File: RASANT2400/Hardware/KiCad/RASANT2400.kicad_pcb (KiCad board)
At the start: 2 copper layers, 60.3 x 51.4 mm, 0 parts

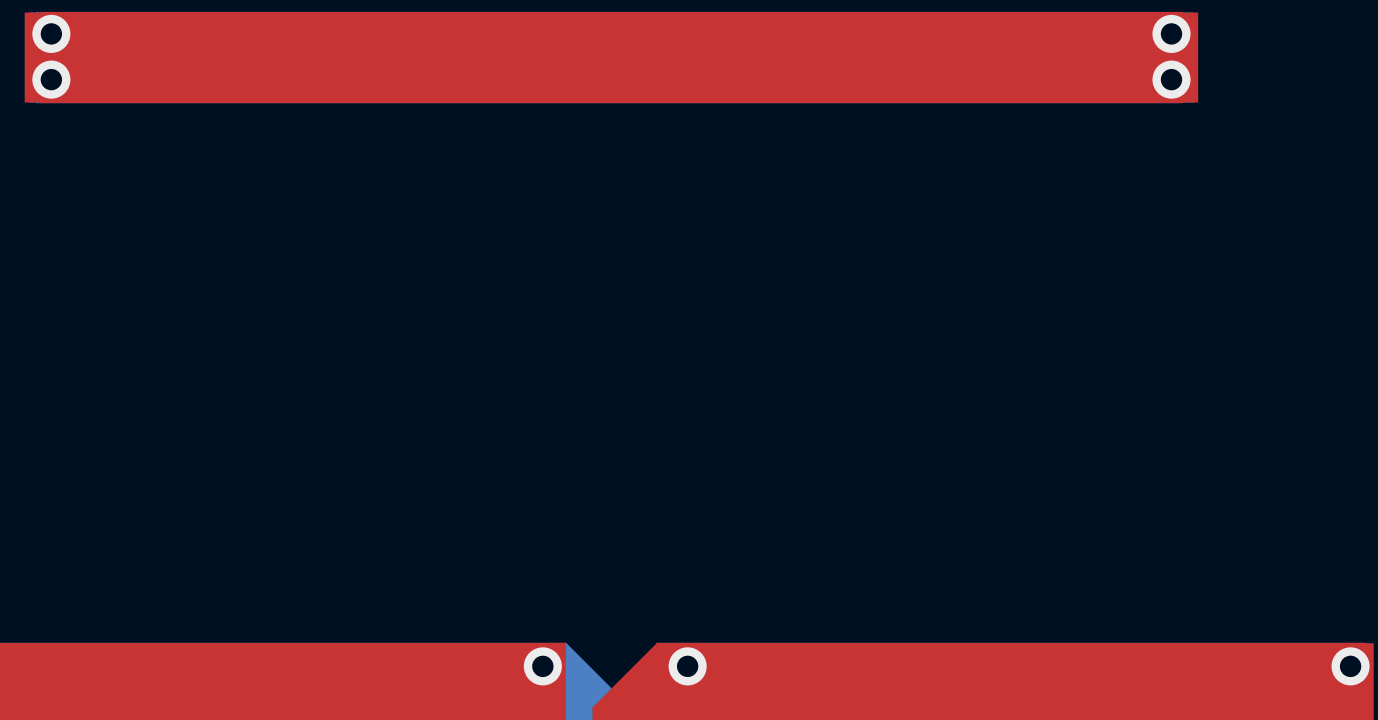
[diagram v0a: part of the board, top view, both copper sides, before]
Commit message: Changed license to CERN Open Hardware Licence Version 2 - Strongly Reciprocal. Changed position of the logos on PCB.
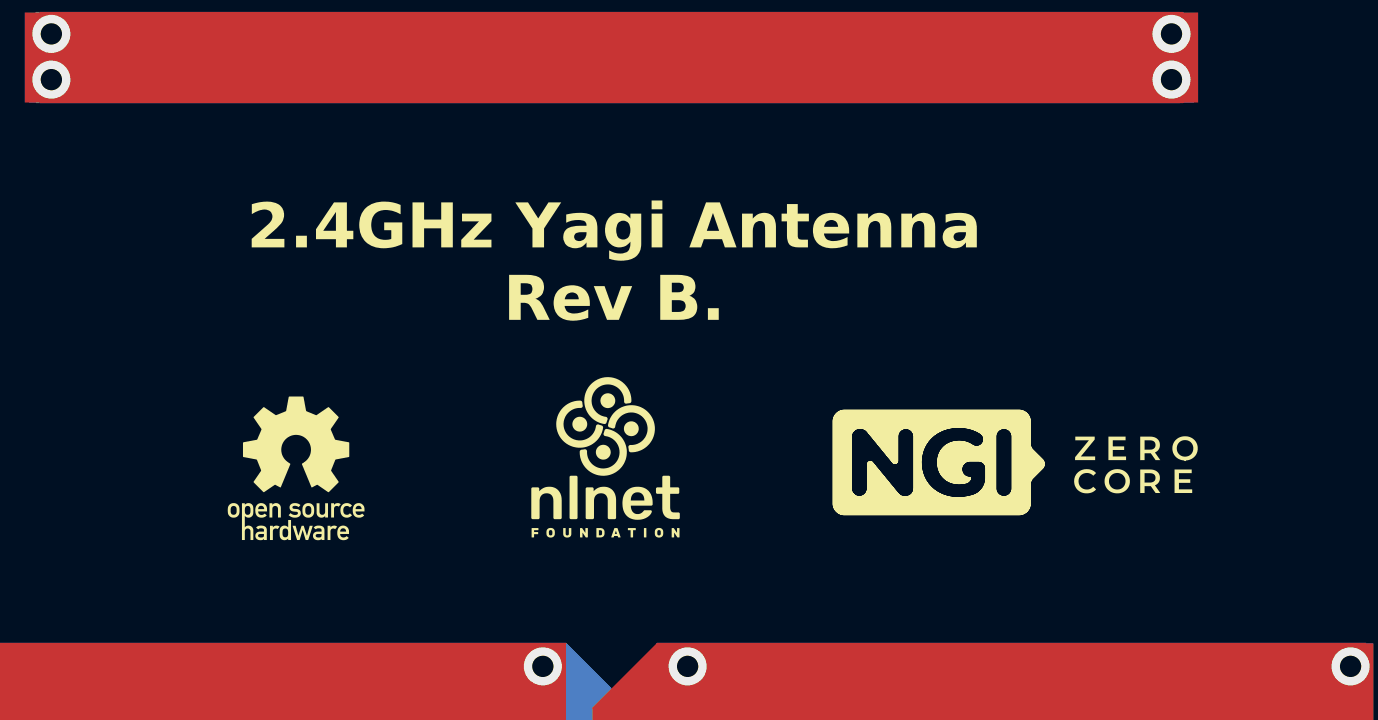
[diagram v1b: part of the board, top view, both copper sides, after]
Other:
- board text added: "2.4GHz Yagi Antenna Rev B."
- board text removed: "2.4GHz Antenna"
